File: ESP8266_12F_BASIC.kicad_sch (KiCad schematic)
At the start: 34 parts, among them J1 Conn_01x02_Male, Q1 BC547, U1 ESP-12F, U2 AP1117-33

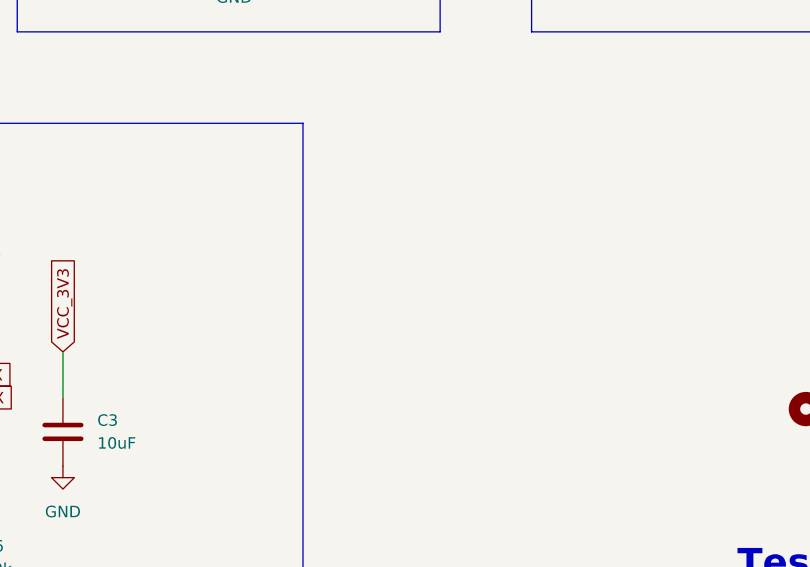
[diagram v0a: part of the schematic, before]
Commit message: fixed header position
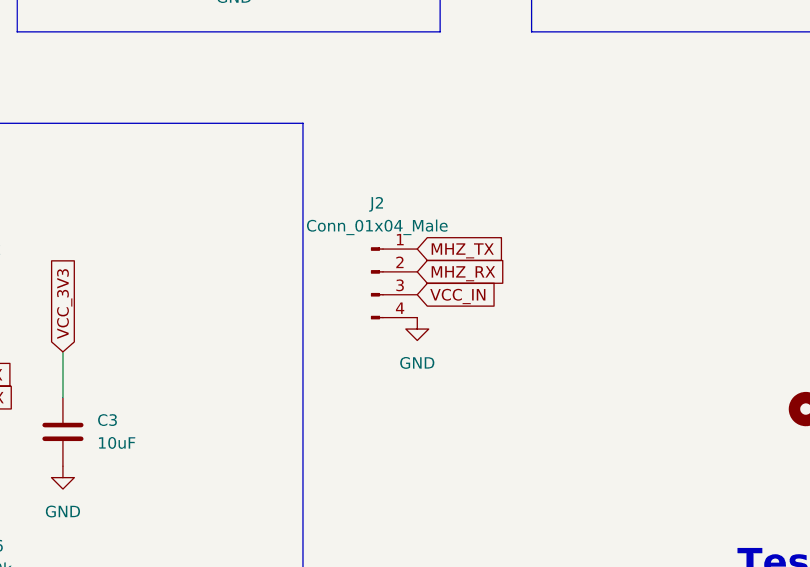
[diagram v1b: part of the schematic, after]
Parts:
- added J2: Conn_01x04_Male, Connector_JST:JST_XH_B4B-XH-A_1x04_P2.50mm_Vertical, symbol Connector:Conn_01x04_Male
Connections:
- net GND: now also J2.4 (Pin_4)
- net MHZ_RX: now also J2.2 (Pin_2)
- net MHZ_TX: now also J2.1 (Pin_1)
- net VCC_IN: now also J2.3 (Pin_3)
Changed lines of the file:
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@@
+    )
+  )
+  (global_label "MHZ_RX" (shape input) (at 151.13 92.71 0) (fields_autoplaced)
+    (effects (font (size 1.27 1.27)) (justify left))
+    (property "Intersheet References" "${INTERSHEET_REFS}" (id 0) (at 160.9817 92.6306 0)
+      (effects (font (size 1.27 1.27)) (justify left) hide)
     )
   )
@@
     )
   )
+  (global_label "MHZ_TX" (shape input) (at 151.13 90.17 0) (fields_autoplaced)
+    (effects (font (size 1.27 1.27)) (justify left))
+    (property "Intersheet References" "${INTERSHEET_REFS}" (id 0) (at 160.6793 90.0906 0)
+      (effects (font (size 1.27 1.27)) (justify left) hide)
+    )
+  )
   (global_label "D1_IN" (shape input) (at 29.21 173.99 180) (fields_autoplaced)
     (effects (font (size 1.27 1.27)) (justify right))
@@
     (property "Intersheet References" "${INTERSHEET_REFS}" (id 0) (at 241.2206 154.1479 90)
       (effects (font (size 1.27 1.27)) (justify right) hide)
+    )
+  )
+  (global_label "VCC_IN" (shape input) (at 151.13 95.25 0) (fields_autoplaced)
+    (effects (font (size 1.27 1.27)) (justify left))
+    (property "Intersheet References" "${INTERSHEET_REFS}" (id 0) (at 160.0745 95.1706 0)
+      (effects (font (size 1.27 1.27)) (justify left) hide)
     )
   )
@@
     )
     (property "Datasheet" "" (id 3) (at 97.79 163.83 0)
+      (effects (font (size 1.27 1.27)) hide)
+    )
+    (pin "1")
+  )
+  (symbol (lib_id "power:GND") (at 151.13 97.79 0) (unit 1)
+    (in_bom yes) (on_board yes) (fields_autoplaced)
+    (property "Reference" "#PWR08" (id 0) (at 151.13 104.14 0)
+      (effects (font (size 1.27 1.27)) hide)
+    )
+    (property "Value" "GND" (id 1) (at 151.13 102.87 0))
+    (property "Footprint" "" (id 2) (at 151.13 97.79 0)
+      (effects (font (size 1.27 1.27)) hide)
+    )
+    (property "Datasheet" "" (id 3) (at 151.13 97.79 0)
       (effects (font (size 1.27 1.27)) hide)
     )
@@
     (pin "2")
   )
+  (symbol (lib_id "Connector:Conn_01x04_Male") (at 146.05 92.71 0) (unit 1)
+    (in_bom yes) (on_board yes) (fields_autoplaced)
+    (property "Reference" "J2" (id 0) (at 146.685 85.09 0))
+    (property "Value" "Conn_01x04_Male" (id 1) (at 146.685 87.63 0))
+    (property "Footprint" "Connector_JST:JST_XH_B4B-XH-A_1x04_P2.50mm_Vertical" (id 2) (at 146.05 92.71 0)
+      (effects (font (size 1.27 1.27)) hide)
+    )
+    (property "Datasheet" "~" (id 3) (at 146.05 92.71 0)
+      (effects (font (size 1.27 1.27)) hide)
+    )
+    (pin "1")
+    (pin "2")
+    (pin "3")
+    (pin "4")
+  )
   (symbol (lib_id "LED:WS2812B") (at 40.64 173.99 0) (unit 1)
     (in_bom yes) (on_board yes)
@@
       (reference "#PWR07") (unit 1) (value "GND") (footprint "")
     )
+    (path "/85df620d-edf4-4420-b05d-3fba08c692a9"
+      (reference "#PWR08") (unit 1) (value "GND") (footprint "")
+    )
     (path "/1ba80035-2558-4bbd-9e48-d22aeb869b13"
       (reference "#PWR09") (unit 1) (value "GND") (footprint "")
@@
       (reference "J1") (unit 1) (value "Conn_01x02_Male") (footprint "Connector_JST:JST_XH_B2B-XH-A_1x02_P2.50mm_Vertical")
     )
+    (path "/e0ee2b78-a7d5-4d4c-a1fc-68c32aabe149"
+      (reference "J2") (unit 1) (value "Conn_01x04_Male") (footprint "Connector_JST:JST_XH_B4B-XH-A_1x04_P2.50mm_Vertical")
+    )
     (path "/3f208147-317d-49ec-8633-535274ffeeca"

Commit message: major fixes
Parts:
- added J3: Conn_01x05_Female, Connector_PinHeader_2.54mm:PinHeader_1x05_P2.54mm_Vertical, symbol Connector:Conn_01x05_Female
- R2: value 100k -> 220k
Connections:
- net ESP_ADC: now also R1.1, R2.2; no longer R1.2, R2.1
- net GND: now also R1.2; no longer R2.2
- net VCC_3V3: now also R2.1; no longer R1.1
- net GPIO2: now reaches U1.17 (GPIO2)
- net GPIO2: now also J3.2 (Pin_2)
- net GPIO3: now reaches U1.21 (GPIO3/RXD)
- net GPIO3: now also J3.3 (Pin_3)
- net GPIO1: now reaches U1.22 (GPIO1/TXD)
- net GPIO1: now also J3.1 (Pin_1)
- net GPIO16: now reaches U1.4 (GPIO16)
- net GPIO16: now also J3.5 (Pin_5)
- net GPIO14: now reaches U1.5 (GPIO14)
- net GPIO14: now also J3.4 (Pin_4)
- no-connect marks 12 -> 7
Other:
- note added: "U_adc = (3,3V / 320kOhm) * R_ldr => U_adc_max = 1,031V U_adc_min ~ 0,01V"
- moved on the sheet: J2, R1, R6

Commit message: caps added and move also added new picture
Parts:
- added C4: 100nF, Capacitor_SMD:C_1206_3216Metric_Pad1.33x1.80mm_HandSolder, symbol Device:C_Small
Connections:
- net GND: now also C4.2
- net VCC_3V3: now also C4.1
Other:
- moved on the sheet: J3
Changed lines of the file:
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@@
   (junction (at 76.2 48.26) (diameter 0) (color 0 0 0 0)
   )
+  (junction (at 111.76 114.3) (diameter 0) (color 0 0 0 0)
+  )
   (junction (at 73.66 163.83) (diameter 0) (color 0 0 0 0)
   )
   (junction (at 55.88 166.37) (diameter 0) (color 0 0 0 0)
+  )
+  (junction (at 111.76 104.14) (diameter 0) (color 0 0 0 0)
   )
   (junction (at 33.02 44.45) (diameter 0) (color 0 0 0 0)
@@
     (stroke (width 0) (type default) (color 0 0 0 0))
   )
+  (wire (pts (xy 124.46 113.03) (xy 124.46 114.3))
+    (stroke (width 0) (type default) (color 0 0 0 0))
+  )
   (wire (pts (xy 177.8 44.45) (xy 181.61 44.45))
     (stroke (width 0) (type default) (color 0 0 0 0))
@@
     (stroke (width 0) (type default) (color 0 0 0 0))
   )
+  (wire (pts (xy 111.76 115.57) (xy 111.76 114.3))
+    (stroke (width 0) (type default) (color 0 0 0 0))
+  )
   (wire (pts (xy 99.06 83.82) (xy 78.74 83.82))
     (stroke (width 0) (type default) (color 0 0 0 0))
@@
     (stroke (width 0) (type default) (color 0 0 0 0))
   )
-  (wire (pts (xy 111.76 101.6) (xy 111.76 106.68))
+  (wire (pts (xy 111.76 101.6) (xy 111.76 104.14))
+    (stroke (width 0) (type default) (color 0 0 0 0))
+  )
+  (wire (pts (xy 124.46 107.95) (xy 124.46 104.14))
     (stroke (width 0) (type default) (color 0 0 0 0))
   )
@@
     (stroke (width 0) (type default) (color 0 0 0 0))
   )
+  (wire (pts (xy 111.76 104.14) (xy 111.76 106.68))
+    (stroke (width 0) (type default) (color 0 0 0 0))
+  )
   (polyline (pts (xy 154.94 138.43) (xy 17.78 138.43))
     (stroke (width 0) (type default) (color 0 0 0 0))
@@
     (stroke (width 0) (type default) (color 0 0 0 0))
   )
+  (wire (pts (xy 124.46 104.14) (xy 111.76 104.14))
+    (stroke (width 0) (type default) (color 0 0 0 0))
+  )
   (wire (pts (xy 93.98 111.76) (xy 96.52 111.76))
     (stroke (width 0) (type default) (color 0 0 0 0))
@@
   )
   (polyline (pts (xy 163.83 22.86) (xy 163.83 66.04))
+    (stroke (width 0) (type default) (color 0 0 0 0))
+  )
+  (wire (pts (xy 111.76 114.3) (xy 124.46 114.3))
     (stroke (width 0) (type default) (color 0 0 0 0))
   )
@@
     )
   )
-  (global_label "GPIO2" (shape input) (at 128.27 113.03 180) (fields_autoplaced)
-    (effects (font (size 1.27 1.27)) (justify right))
-    (property "Intersheet References" "${INTERSHEET_REFS}" (id 0) (at 120.1721 113.1094 0)
+  (global_label "GPIO2" (shape input) (at 125.73 125.73 180) (fields_autoplaced)
+    (effects (font (size 1.27 1.27)) (justify right))
+    (property "Intersheet References" "${INTERSHEET_REFS}" (id 0) (at 117.6321 125.8094 0)
       (effects (font (size 1.27 1.27)) (justify right) hide)
     )
@@
     )
   )
-  (global_label "GPIO1" (shape input) (at 128.27 110.49 180) (fields_autoplaced)
-    (effects (font (size 1.27 1.27)) (justify right))
-    (property "Intersheet References" "${INTERSHEET_REFS}" (id 0) (at 120.1721 110.5694 0)
-      (effects (font (size 1.27 1.27)) (justify right) hide)
-    )
-  )
-  (global_label "GPIO14" (shape input) (at 128.27 118.11 180) (fields_autoplaced)
-    (effects (font (size 1.27 1.27)) (justify right))
-    (property "Intersheet References" "${INTERSHEET_REFS}" (id 0) (at 118.9626 118.1894 0)
+  (global_label "GPIO1" (shape input) (at 125.73 123.19 180) (fields_autoplaced)
+    (effects (font (size 1.27 1.27)) (justify right))
+    (property "Intersheet References" "${INTERSHEET_REFS}" (id 0) (at 117.6321 123.2694 0)
+      (effects (font (size 1.27 1.27)) (justify right) hide)
+    )
+  )
+  (global_label "GPIO14" (shape input) (at 125.73 130.81 180) (fields_autoplaced)
+    (effects (font (size 1.27 1.27)) (justify right))
+    (property "Intersheet References" "${INTERSHEET_REFS}" (id 0) (at 116.4226 130.8894 0)
       (effects (font (size 1.27 1.27)) (justify right) hide)
     )
@@
     )
   )
-  (global_label "GPIO3" (shape input) (at 128.27 115.57 180) (fields_autoplaced)
-    (effects (font (size 1.27 1.27)) (justify right))
-    (property "Intersheet References" "${INTERSHEET_REFS}" (id 0) (at 120.1721 115.6494 0)
+  (global_label "GPIO3" (shape input) (at 125.73 128.27 180) (fields_autoplaced)
+    (effects (font (size 1.27 1.27)) (justify right))
+    (property "Intersheet References" "${INTERSHEET_REFS}" (id 0) (at 117.6321 128.3494 0)
       (effects (font (size 1.27 1.27)) (justify right) hide)
     )
@@
     )
   )
-  (global_label "GPIO16" (shape input) (at 128.27 120.65 180) (fields_autoplaced)
-    (effects (font (size 1.27 1.27)) (justify right))
-    (property "Intersheet References" "${INTERSHEET_REFS}" (id 0) (at 118.9626 120.7294 0)
+  (global_label "GPIO16" (shape input) (at 125.73 133.35 180) (fields_autoplaced)
+    (effects (font (size 1.27 1.27)) (justify right))
+    (property "Intersheet References" "${INTERSHEET_REFS}" (id 0) (at 116.4226 133.4294 0)
       (effects (font (size 1.27 1.27)) (justify right) hide)
     )
@@
     (pin "2")
   )
-  (symbol (lib_id "Connector:Conn_01x05_Female") (at 133.35 115.57 0) (unit 1)
-    (in_bom yes) (on_board yes) (fields_autoplaced)
-    (property "Reference" "J3" (id 0) (at 134.62 114.2999 0)
-      (effects (font (size 1.27 1.27)) (justify left))
-    )
-    (property "Value" "Conn_01x05_Female" (id 1) (at 134.62 116.8399 0)
-      (effects (font (size 1.27 1.27)) (justify left))
-    )
-    (property "Footprint" "Connector_PinHeader_2.54mm:PinHeader_1x05_P2.54mm_Vertical" (id 2) (at 133.35 115.57 0)
-      (effects (font (size 1.27 1.27)) hide)
-    )
-    (property "Datasheet" "~" (id 3) (at 133.35 115.57 0)
+  (symbol (lib_id "Connector:Conn_01x05_Female") (at 130.81 128.27 0) (unit 1)
+    (in_bom yes) (on_board yes) (fields_autoplaced)
+    (property "Reference" "J3" (id 0) (at 132.08 126.9999 0)
+      (effects (font (size 1.27 1.27)) (justify left))
+    )
+    (property "Value" "Conn_01x05_Female" (id 1) (at 132.08 129.5399 0)
+      (effects (font (size 1.27 1.27)) (justify left))
+    )
+    (property "Footprint" "Connector_PinHeader_2.54mm:PinHeader_1x05_P2.54mm_Vertical" (id 2) (at 130.81 128.27 0)
+      (effects (font (size 1.27 1.27)) hide)
+    )
+    (property "Datasheet" "~" (id 3) (at 130.81 128.27 0)
       (effects (font (size 1.27 1.27)) hide)
     )
@@
     (pin "4")
   )
+  (symbol (lib_id "Device:C_Small") (at 124.46 110.49 0) (unit 1)
+    (in_bom yes) (on_board yes) (fields_autoplaced)
+    (property "Reference" "C4" (id 0) (at 127 109.2262 0)
+      (effects (font (size 1.27 1.27)) (justify left))
+    )
+    (property "Value" "100nF" (id 1) (at 127 111.7662 0)
+      (effects (font (size 1.27 1.27)) (justify left))
+    )
+    (property "Footprint" "Capacitor_SMD:C_1206_3216Metric_Pad1.33x1.80mm_HandSolder" (id 2) (at 124.46 110.49 0)
+      (effects (font (size 1.27 1.27)) hide)
+    )
+    (property "Datasheet" "~" (id 3) (at 124.46 110.49 0)
+      (effects (font (size 1.27 1.27)) hide)
+    )
+    (pin "1")
+    (pin "2")
+  )
   (symbol (lib_id "Device:R_Small") (at 123.19 38.1 180) (unit 1)
     (in_bom yes) (on_board yes)
@@
     (pin "2")
   )
-  (symbol (lib_id "power:GND") (at 111.76 114.3 0) (unit 1)
-    (in_bom yes) (on_board yes) (fields_autoplaced)
-    (property "Reference" "#PWR06" (id 0) (at 111.76 120.65 0)
-      (effects (font (size 1.27 1.27)) hide)
-    )
-    (property "Value" "GND" (id 1) (at 111.76 119.38 0))
-    (property "Footprint" "" (id 2) (at 111.76 114.3 0)
-      (effects (font (size 1.27 1.27)) hide)
-    )
-    (property "Datasheet" "" (id 3) (at 111.76 114.3 0)
+  (symbol (lib_id "power:GND") (at 111.76 115.57 0) (unit 1)
+    (in_bom yes) (on_board yes) (fields_autoplaced)
+    (property "Reference" "#PWR06" (id 0) (at 111.76 121.92 0)
+      (effects (font (size 1.27 1.27)) hide)
+    )
+    (property "Value" "GND" (id 1) (at 111.76 120.65 0))
+    (property "Footprint" "" (id 2) (at 111.76 115.57 0)
+      (effects (font (size 1.27 1.27)) hide)
+    )
+    (property "Datasheet" "" (id 3) (at 111.76 115.57 0)
       (effects (font (size 1.27 1.27)) hide)
     )
@@
       (reference "C3") (unit 1) (value "10uF") (footprint "Capacitor_THT:CP_Radial_D6.3mm_P2.50mm")
     )
+    (path "/98303ac1-b7d5-40e4-aac5-5ff68116461f"
+      (reference "C4") (unit 1) (value "100nF") (footprint "Capacitor_SMD:C_1206_3216Metric_Pad1.33x1.80mm_HandSolder")
+    )
     (path "/9fbcf246-9897-43b2-ba86-188b08b53625"
